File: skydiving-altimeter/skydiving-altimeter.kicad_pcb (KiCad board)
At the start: 2 copper layers, 26.3 x 45.1 mm, 23 parts, among them J1 Conn_ARM_JTAG_SWD_10, J2 Battery JST Connector, J3 Conn_01x03, U1 STM32F103C8Tx, U2 BMP581, U4 RP400N501A-TR-FE, U5 LDL1117S33R

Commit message: Began adding 10 ohm current limiting resistors
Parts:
- added D1: LED, Diode_SMD:D_0603_1608Metric, F.Cu at (108.6, 102.9)
- added R3: 500, Resistor_SMD:R_0805_2012Metric, F.Cu at (106.0, 102.9)
- added R4: 10, Resistor_SMD:R_0805_2012Metric, F.Cu at (133.7, 101.2)
- added R5: 10, Resistor_SMD:R_0805_2012Metric, F.Cu at (133.7, 104.1)
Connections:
- C7 pad 2: +3V3 -> Net-(U2-VDD)
- C8 pad 2: +3V3 -> Net-(U2-SDO)
- U2 pad 1: +3V3 -> Net-(U2-SDO)
- U2 pad 10: +3V3 -> Net-(U2-VDD)
- U2 pad 5: +3V3 -> Net-(U2-SDO)
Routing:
- net +3V3: track 118.9 -> 124.3 mm
- net Net-(D1-A): track 0.00 -> 2.59 mm
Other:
- board text added: "3.3V"

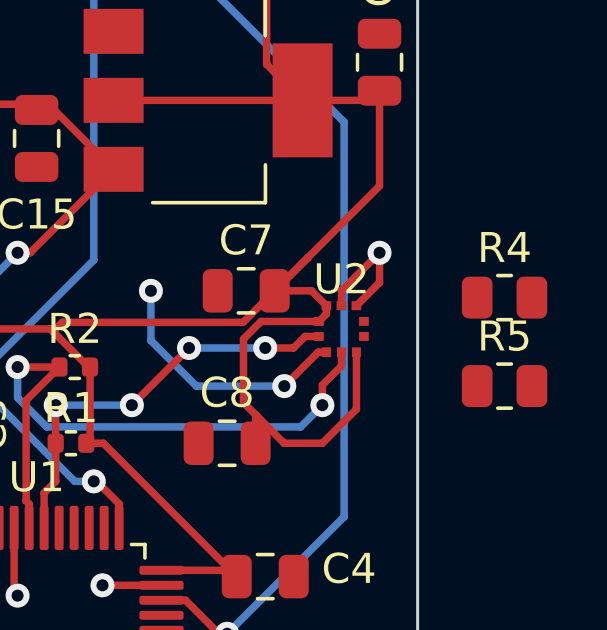
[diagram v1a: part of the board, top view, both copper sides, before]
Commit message: Fixed CSB pin routing
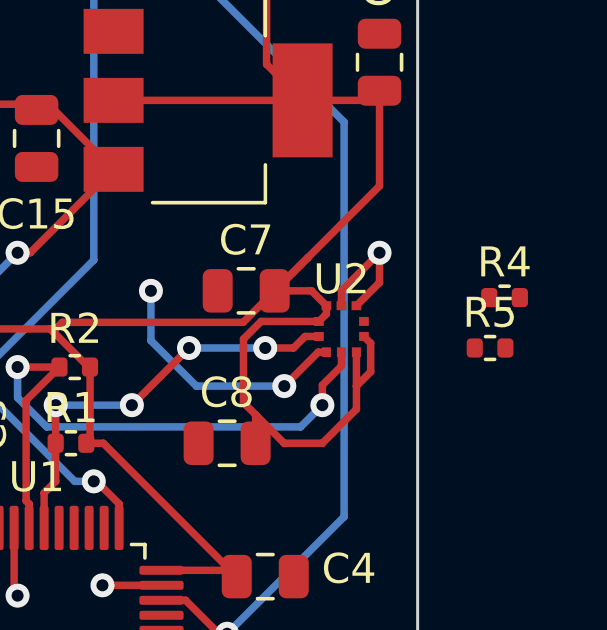
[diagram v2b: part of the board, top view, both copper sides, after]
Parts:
- R4, R5: footprint Resistor_SMD:R_0805_2012Metric -> Resistor_SMD:R_0402_1005Metric
- moved R5 1.36 mm to (133.2, 102.9)
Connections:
- U2 pad 6: unconnected-(U2-CSB-Pad6) -> +3V3
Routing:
- net +3V3: track 124.3 -> 126.2 mm

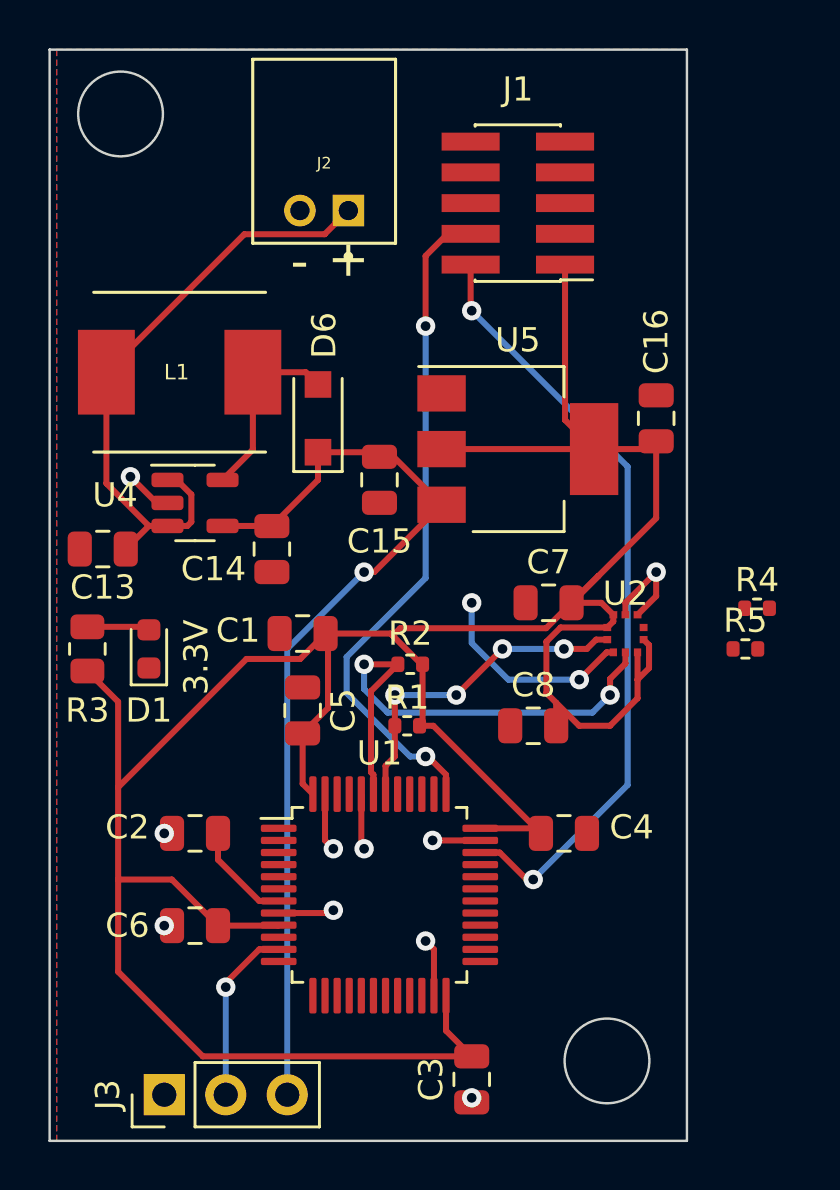
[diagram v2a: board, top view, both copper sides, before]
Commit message: Switched most components to 0402
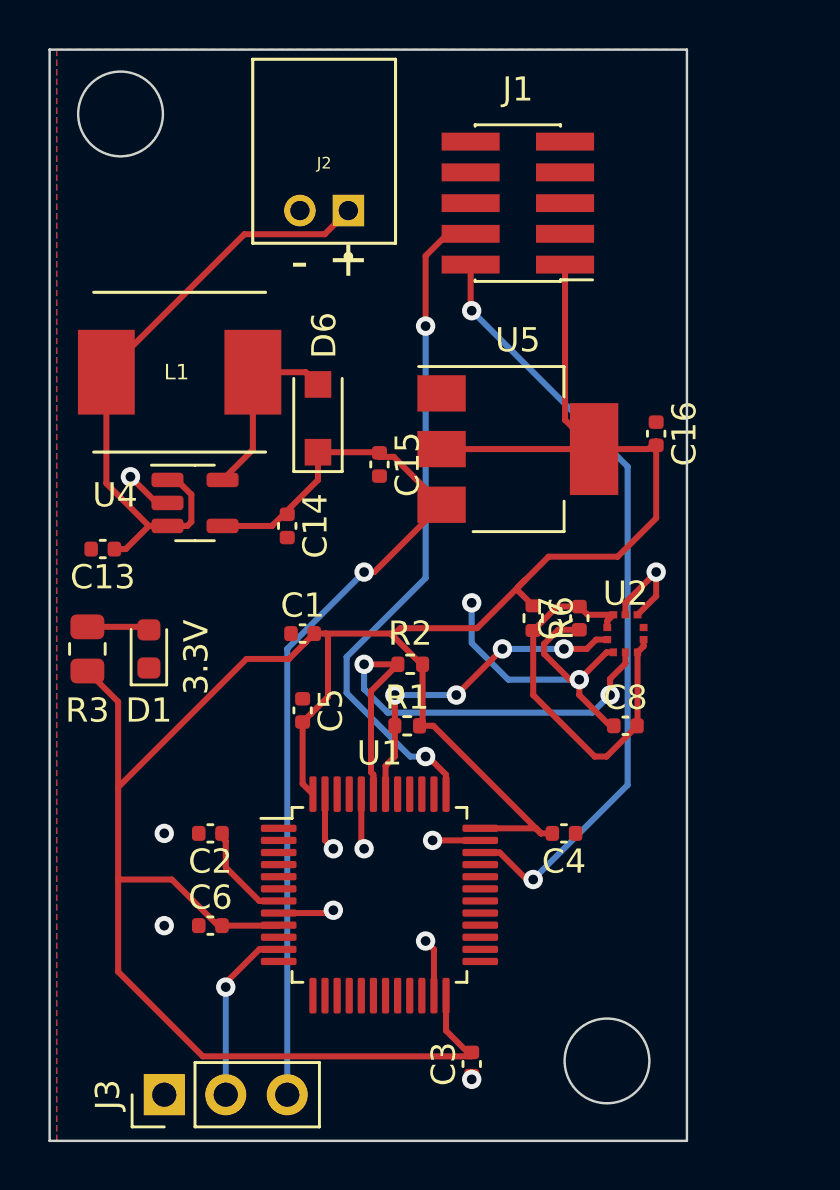
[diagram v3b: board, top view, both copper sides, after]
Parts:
- removed R4, R5: 10, Resistor_SMD:R_0402_1005Metric
- added R6: 10, Resistor_SMD:R_0402_1005Metric, F.Cu at (124.5, 101.6)
- C1, C13, C14, C15, C16, C2, C3, C4, C5, C6, C7, C8: footprint Capacitor_SMD:C_0805_2012Metric -> Capacitor_SMD:C_0402_1005Metric
- moved C8 3.81 mm to (128.3, 106.0)
- moved C7 1.42 mm to (126.4, 101.6), turned to 90 degrees
- moved C14 1.15 mm to (114.3, 97.8)
- moved C15 0.64 mm to (118.1, 95.2)
- moved C16 0.64 mm to (129.5, 94.0)
- moved C2 0.64 mm to (111.1, 110.5)
- moved C3 0.64 mm to (121.9, 120.0)
- moved C6 0.64 mm to (111.1, 114.3)
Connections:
- C7 pad 2: Net-(U2-VDD) -> Net-(U2-CSB)
- C8 pad 2: Net-(U2-SDO) -> Net-(U2-CSB)
- U2 pad 1: Net-(U2-SDO) -> Net-(U2-CSB)
- U2 pad 10: Net-(U2-VDD) -> Net-(U2-CSB)
- U2 pad 5: Net-(U2-SDO) -> Net-(U2-CSB)
- U2 pad 6: +3V3 -> Net-(U2-CSB)
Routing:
- net Net-(U2-CSB): track 0.00 -> 16.7 mm
- net +3V3: track 126.2 -> 109.6 mm
- net GND: track 26.3 -> 32.9 mm
